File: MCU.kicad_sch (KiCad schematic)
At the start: 35 parts, among them J301 Conn_01x04_Pin, SW301 SW_Push, SW302 SW_Push, U301 STM32F405RGTx, Y301 24MHz

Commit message: refactor: change name from FeroFly405 to FeroFlyF405
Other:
- title: FeroFly405 -> FeroFlyF405
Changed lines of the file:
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@@
 	(paper "A4")
 	(title_block
-		(title "FeroFly405")
+		(title "FeroFlyF405")
 		(date "2026-07-22")
 		(rev "1")
-		(comment 3 "GitHub: https://github.com/Ozonised/FeroFly405")
+		(comment 3 "GitHub: https://github.com/Ozonised/FeroFlyF405")
 		(comment 4 "Designed by: Farhan Khan")
 	)
@@
 		)
 		(instances
-			(project "FeroFly"
+			(project "FeroFlyF405"
 				(path "/8fea5468-8d8d-4bdb-afc0-e65b62c92669/5f464b6b-c1a5-4802-8c09-16302411334a"
 					(reference "#PWR0314")
@@
 		)
 		(instances
-			(project "FeroFly"
+			(project "FeroFlyF405"
 				(path "/8fea5468-8d8d-4bdb-afc0-e65b62c92669/5f464b6b-c1a5-4802-8c09-16302411334a"
 					(reference "#PWR0307")
@@
 		)
 		(instances
-			(project "FeroFly"
+			(project "FeroFlyF405"
 				(path "/8fea5468-8d8d-4bdb-afc0-e65b62c92669/5f464b6b-c1a5-4802-8c09-16302411334a"
 					(reference "C307")
@@
 		)
 		(instances
-			(project "FeroFly"
+			(project "FeroFlyF405"
 				(path "/8fea5468-8d8d-4bdb-afc0-e65b62c92669/5f464b6b-c1a5-4802-8c09-16302411334a"
 					(reference "#PWR0305")
@@
 		)
 		(instances
-			(project "FeroFly"
+			(project "FeroFlyF405"
 				(path "/8fea5468-8d8d-4bdb-afc0-e65b62c92669/5f464b6b-c1a5-4802-8c09-16302411334a"
 					(reference "#PWR0303")
@@
 		)
 		(instances
-			(project "FeroFly"
+			(project "FeroFlyF405"
 				(path "/8fea5468-8d8d-4bdb-afc0-e65b62c92669/5f464b6b-c1a5-4802-8c09-16302411334a"
 					(reference "R303")
@@
 		)
 		(instances
-			(project "FeroFly"
+			(project "FeroFlyF405"
 				(path "/8fea5468-8d8d-4bdb-afc0-e65b62c92669/5f464b6b-c1a5-4802-8c09-16302411334a"
 					(reference "#PWR0304")
@@
 		)
 		(instances
-			(project "FeroFly"
+			(project "FeroFlyF405"
 				(path "/8fea5468-8d8d-4bdb-afc0-e65b62c92669/5f464b6b-c1a5-4802-8c09-16302411334a"
 					(reference "SW302")
@@
 		)
 		(instances
-			(project "FeroFly"
+			(project "FeroFlyF405"
 				(path "/8fea5468-8d8d-4bdb-afc0-e65b62c92669/5f464b6b-c1a5-4802-8c09-16302411334a"
 					(reference "R313")
@@
 		)
 		(instances
-			(project "FeroFly"
+			(project "FeroFlyF405"
 				(path "/8fea5468-8d8d-4bdb-afc0-e65b62c92669/5f464b6b-c1a5-4802-8c09-16302411334a"
 					(reference "R305")
@@
 		)
 		(instances
-			(project "FeroFly"
+			(project "FeroFlyF405"
 				(path "/8fea5468-8d8d-4bdb-afc0-e65b62c92669/5f464b6b-c1a5-4802-8c09-16302411334a"
 					(reference "R315")
@@
 		)
 		(instances
-			(project "FeroFly"
+			(project "FeroFlyF405"
 				(path "/8fea5468-8d8d-4bdb-afc0-e65b62c92669/5f464b6b-c1a5-4802-8c09-16302411334a"
 					(reference "#PWR0313")
@@
 		)
 		(instances
-			(project "FeroFly"
+			(project "FeroFlyF405"
 				(path "/8fea5468-8d8d-4bdb-afc0-e65b62c92669/5f464b6b-c1a5-4802-8c09-16302411334a"
 					(reference "C314")
@@
 		)
 		(instances
-			(project "FeroFly"
+			(project "FeroFlyF405"
 				(path "/8fea5468-8d8d-4bdb-afc0-e65b62c92669/5f464b6b-c1a5-4802-8c09-16302411334a"
 					(reference "C308")
@@
 		)
 		(instances
-			(project "FeroFly"
+			(project "FeroFlyF405"
 				(path "/8fea5468-8d8d-4bdb-afc0-e65b62c92669/5f464b6b-c1a5-4802-8c09-16302411334a"
 					(reference "R314")
@@
 		)
 		(instances
-			(project "FeroFly"
+			(project "FeroFlyF405"
 				(path "/8fea5468-8d8d-4bdb-afc0-e65b62c92669/5f464b6b-c1a5-4802-8c09-16302411334a"
 					(reference "R310")
@@
 		)
 		(instances
-			(project "FeroFly"
+			(project "FeroFlyF405"
 				(path "/8fea5468-8d8d-4bdb-afc0-e65b62c92669/5f464b6b-c1a5-4802-8c09-16302411334a"
 					(reference "#PWR0312")
@@
 		)
 		(instances
-			(project "FeroFly"
+			(project "FeroFlyF405"
 				(path "/8fea5468-8d8d-4bdb-afc0-e65b62c92669/5f464b6b-c1a5-4802-8c09-16302411334a"
 					(reference "C302")
@@
 		)
 		(instances
-			(project "FeroFly"
+			(project "FeroFlyF405"
 				(path "/8fea5468-8d8d-4bdb-afc0-e65b62c92669/5f464b6b-c1a5-4802-8c09-16302411334a"
 					(reference "R309")
@@
 		)
 		(instances
-			(project "FeroFly"
+			(project "FeroFlyF405"
 				(path "/8fea5468-8d8d-4bdb-afc0-e65b62c92669/5f464b6b-c1a5-4802-8c09-16302411334a"
 					(reference "#PWR0310")
@@
 		)
 		(instances
-			(project "FeroFly"
+			(project "FeroFlyF405"
 				(path "/8fea5468-8d8d-4bdb-afc0-e65b62c92669/5f464b6b-c1a5-4802-8c09-16302411334a"
 					(reference "C306")
@@
 		)
 		(instances
-			(project "FeroFly"
+			(project "FeroFlyF405"
 				(path "/8fea5468-8d8d-4bdb-afc0-e65b62c92669/5f464b6b-c1a5-4802-8c09-16302411334a"
 					(reference "J301")
@@
 		)
 		(instances
-			(project "FeroFly"
+			(project "FeroFlyF405"
 				(path "/8fea5468-8d8d-4bdb-afc0-e65b62c92669/5f464b6b-c1a5-4802-8c09-16302411334a"
 					(reference "#PWR0309")
@@
 		)
 		(instances
-			(project "FeroFly"
+			(project "FeroFlyF405"
 				(path "/8fea5468-8d8d-4bdb-afc0-e65b62c92669/5f464b6b-c1a5-4802-8c09-16302411334a"
 					(reference "R312")
@@
 		)
 		(instances
-			(project "FeroFly"
+			(project "FeroFlyF405"
 				(path "/8fea5468-8d8d-4bdb-afc0-e65b62c92669/5f464b6b-c1a5-4802-8c09-16302411334a"
 					(reference "R307")
@@
 		)
 		(instances
-			(project "FeroFly"
+			(project "FeroFlyF405"
 				(path "/8fea5468-8d8d-4bdb-afc0-e65b62c92669/5f464b6b-c1a5-4802-8c09-16302411334a"
 					(reference "C313")
@@
 		)
 		(instances
-			(project "FeroFly"
+			(project "FeroFlyF405"
 				(path "/8fea5468-8d8d-4bdb-afc0-e65b62c92669/5f464b6b-c1a5-4802-8c09-16302411334a"
 					(reference "#PWR0315")
@@
 		)
 		(instances
-			(project "FeroFly"
+			(project "FeroFlyF405"
 				(path "/8fea5468-8d8d-4bdb-afc0-e65b62c92669/5f464b6b-c1a5-4802-8c09-16302411334a"
 					(reference "C312")
@@
 		)
 		(instances
-			(project "FeroFly"
+			(project "FeroFlyF405"
 				(path "/8fea5468-8d8d-4bdb-afc0-e65b62c92669/5f464b6b-c1a5-4802-8c09-16302411334a"
 					(reference "C305")
@@
 		)
 		(instances
-			(project "FeroFly"
+			(project "FeroFlyF405"
 				(path "/8fea5468-8d8d-4bdb-afc0-e65b62c92669/5f464b6b-c1a5-4802-8c09-16302411334a"
 					(reference "U301")
@@
 		)
 		(instances
-			(project "FeroFly"
+			(project "FeroFlyF405"
 				(path "/8fea5468-8d8d-4bdb-afc0-e65b62c92669/5f464b6b-c1a5-4802-8c09-16302411334a"
 					(reference "R311")
@@
 		)
 		(instances
-			(project "FeroFly"
+			(project "FeroFlyF405"
 				(path "/8fea5468-8d8d-4bdb-afc0-e65b62c92669/5f464b6b-c1a5-4802-8c09-16302411334a"
 					(reference "#PWR0301")
@@
 		)
 		(instances
-			(project "FeroFly"
+			(project "FeroFlyF405"
 				(path "/8fea5468-8d8d-4bdb-afc0-e65b62c92669/5f464b6b-c1a5-4802-8c09-16302411334a"
 					(reference "#PWR0306")
@@
 		)
 		(instances
-			(project "FeroFly"
+			(project "FeroFlyF405"
 				(path "/8fea5468-8d8d-4bdb-afc0-e65b62c92669/5f464b6b-c1a5-4802-8c09-16302411334a"
 					(reference "C303")
@@
 		)
 		(instances
-			(project "FeroFly"
+			(project "FeroFlyF405"
 				(path "/8fea5468-8d8d-4bdb-afc0-e65b62c92669/5f464b6b-c1a5-4802-8c09-16302411334a"
 					(reference "#PWR0308")
@@
 		)
 		(instances
-			(project "FeroFly"
+			(project "FeroFlyF405"
 				(path "/8fea5468-8d8d-4bdb-afc0-e65b62c92669/5f464b6b-c1a5-4802-8c09-16302411334a"
 					(reference "R302")
@@
 		)
 		(instances
-			(project "FeroFly"
+			(project "FeroFlyF405"
 				(path "/8fea5468-8d8d-4bdb-afc0-e65b62c92669/5f464b6b-c1a5-4802-8c09-16302411334a"
 					(reference "C301")
@@
 		)
 		(instances
-			(project "FeroFly"
+			(project "FeroFlyF405"
 				(path "/8fea5468-8d8d-4bdb-afc0-e65b62c92669/5f464b6b-c1a5-4802-8c09-16302411334a"
 					(reference "SW301")
@@
 		)
 		(instances
-			(project "FeroFly"
+			(project "FeroFlyF405"
 				(path "/8fea5468-8d8d-4bdb-afc0-e65b62c92669/5f464b6b-c1a5-4802-8c09-16302411334a"
 					(reference "Y301")
@@
 		)
 		(instances
-			(project "FeroFly"
+			(project "FeroFlyF405"
 				(path "/8fea5468-8d8d-4bdb-afc0-e65b62c92669/5f464b6b-c1a5-4802-8c09-16302411334a"
 					(reference "#PWR0302")
@@
 		)
 		(instances
-			(project "FeroFly"
+			(project "FeroFlyF405"
 				(path "/8fea5468-8d8d-4bdb-afc0-e65b62c92669/5f464b6b-c1a5-4802-8c09-16302411334a"
 					(reference "C304")
@@
 		)
 		(instances
-			(project "FeroFly"
+			(project "FeroFlyF405"
 				(path "/8fea5468-8d8d-4bdb-afc0-e65b62c92669/5f464b6b-c1a5-4802-8c09-16302411334a"
 					(reference "R316")
@@
 		)
 		(instances
-			(project "FeroFly"
+			(project "FeroFlyF405"
 				(path "/8fea5468-8d8d-4bdb-afc0-e65b62c92669/5f464b6b-c1a5-4802-8c09-16302411334a"
 					(reference "C309")
@@
 		)
 		(instances
-			(project "FeroFly"
+			(project "FeroFlyF405"
 				(path "/8fea5468-8d8d-4bdb-afc0-e65b62c92669/5f464b6b-c1a5-4802-8c09-16302411334a"
 					(reference "R308")
@@
 		)
 		(instances
-			(project "FeroFly"
+			(project "FeroFlyF405"
 				(path "/8fea5468-8d8d-4bdb-afc0-e65b62c92669/5f464b6b-c1a5-4802-8c09-16302411334a"
 					(reference "#PWR0311")
@@
 		)
 		(instances
-			(project "FeroFly"
+			(project "FeroFlyF405"
 				(path "/8fea5468-8d8d-4bdb-afc0-e65b62c92669/5f464b6b-c1a5-4802-8c09-16302411334a"
 					(reference "C311")
@@
 		)
 		(instances
-			(project "FeroFly"
+			(project "FeroFlyF405"
 				(path "/8fea5468-8d8d-4bdb-afc0-e65b62c92669/5f464b6b-c1a5-4802-8c09-16302411334a"
 					(reference "R301")
@@
 		)
 		(instances
-			(project "FeroFly"
+			(project "FeroFlyF405"
 				(path "/8fea5468-8d8d-4bdb-afc0-e65b62c92669/5f464b6b-c1a5-4802-8c09-16302411334a"
 					(reference "R304")
@@
 		)
 		(instances
-			(project "FeroFly"
+			(project "FeroFlyF405"
 				(path "/8fea5468-8d8d-4bdb-afc0-e65b62c92669/5f464b6b-c1a5-4802-8c09-16302411334a"
 					(reference "R306")
@@
 		)
 		(instances
-			(project "FeroFly"
+			(project "FeroFlyF405"
 				(path "/8fea5468-8d8d-4bdb-afc0-e65b62c92669/5f464b6b-c1a5-4802-8c09-16302411334a"
 					(reference "C310")

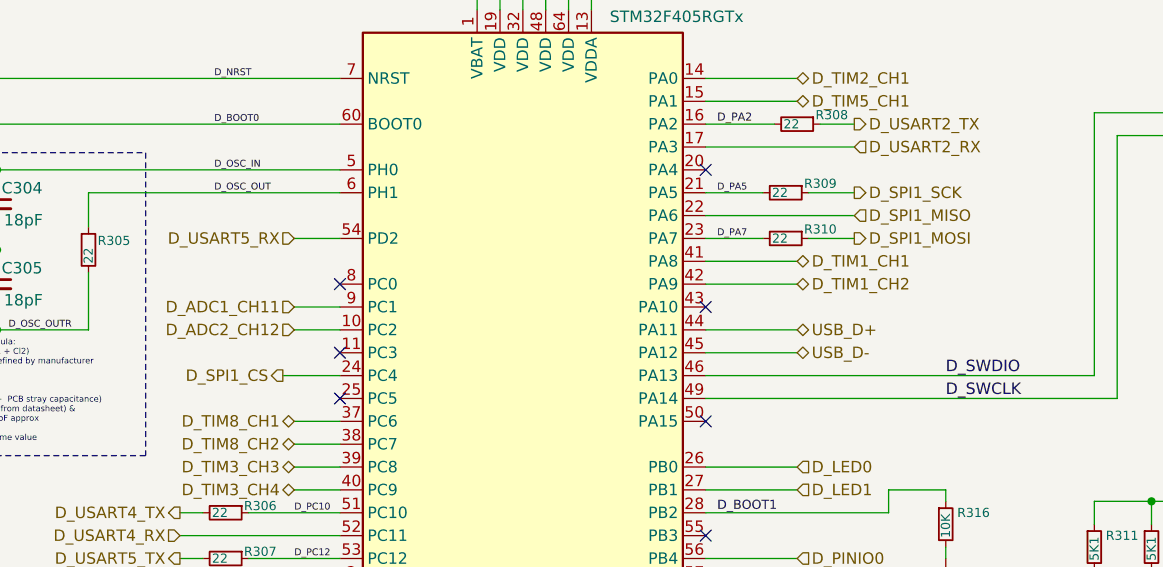
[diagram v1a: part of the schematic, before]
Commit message: refactor(schematic): assign net classes and fix USB net label assingment
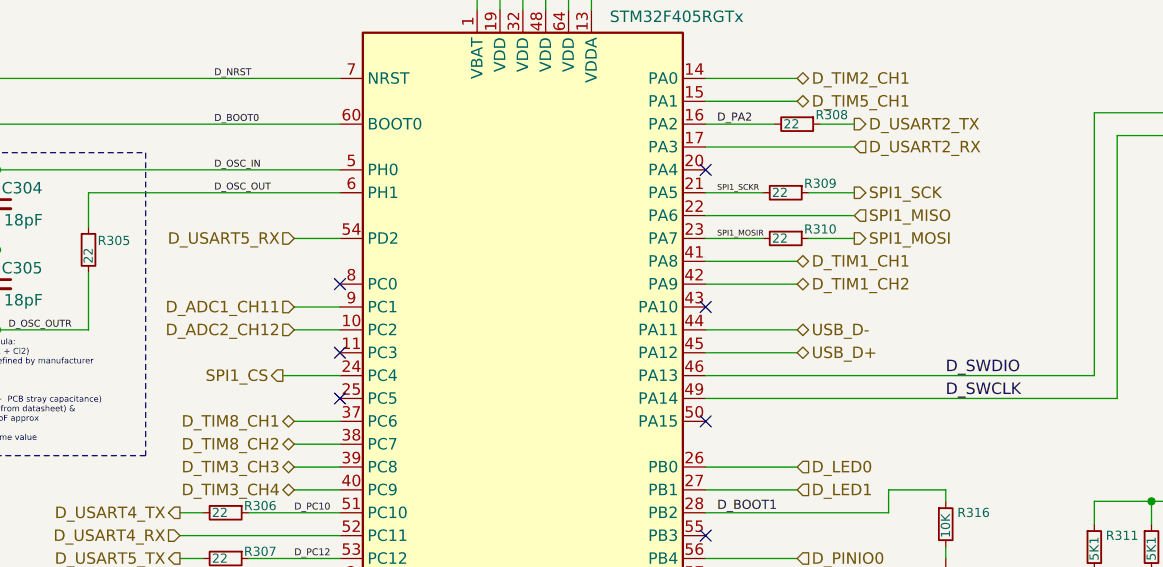
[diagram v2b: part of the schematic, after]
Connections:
- net USB_D+: now also U301.45 (PA12); no longer U301.44 (PA11)
- net USB_D-: now also U301.44 (PA11); no longer U301.45 (PA12)
- net D_PA5 renamed SPI1_SCKR
- net D_PA7 renamed SPI1_MOSIR
- net D_SPI1_CS renamed SPI1_CS
- net D_SPI1_MISO renamed SPI1_MISO
- net D_SPI1_MOSI renamed SPI1_MOSI
- net D_SPI1_SCK renamed SPI1_SCK

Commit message: refactor: change motor output, renamed power nets
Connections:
- net D_ADC1_CH11 is gone; now on net D_LED0: U301.9 (PC1)
- net D_ADC2_CH12 is gone; now on net D_LED1: U301.10 (PC2)
- net D_LED0: no longer U301.26 (PB0)
- net D_LED1: no longer U301.27 (PB1)
- net D_ADC2_CH13: now reaches U301.11 (PC3)
- net D_ADC1_CH10: now reaches U301.8 (PC0)
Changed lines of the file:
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@@
 	)
 	(no_connect
-		(at 134.62 104.14)
+		(at 175.26 119.38)
 	)
 	(no_connect
@@
 	)
 	(no_connect
-		(at 134.62 96.52)
+		(at 175.26 124.46)
 	)
 	(no_connect
-		(at 175.26 124.46)
+		(at 175.26 116.84)
 	)
 	(no_connect
@@
 	(wire
 		(pts
-			(xy 175.26 119.38) (xy 185.42 119.38)
-		)
-		(stroke
-			(width 0)
-			(type default)
-		)
-	)
-	(wire
-		(pts
 			(xy 218.44 123.19) (xy 218.44 120.65)
 		)
@@
 	(wire
 		(pts
+			(xy 129.54 104.14) (xy 134.62 104.14)
+		)
+		(stroke
+			(width 0)
+			(type default)
+		)
+	)
+	(wire
+		(pts
 			(xy 124.46 127) (xy 134.62 127)
 		)
@@
 	(wire
 		(pts
-			(xy 175.26 116.84) (xy 185.42 116.84)
-		)
-		(stroke
-			(width 0)
-			(type default)
-		)
-	)
-	(wire
-		(pts
 			(xy 74.93 78.74) (xy 74.93 97.79)
 		)
@@
 		(pts
 			(xy 60.96 97.79) (xy 63.5 97.79)
+		)
+		(stroke
+			(width 0)
+			(type default)
+		)
+	)
+	(wire
+		(pts
+			(xy 129.54 96.52) (xy 134.62 96.52)
 		)
 		(stroke
@@
 		)
 	)
+	(hierarchical_label "D_LED0"
+		(shape input)
+		(at 129.54 99.06 180)
+		(effects
+			(font
+				(size 1.27 1.27)
+			)
+			(justify right)
+		)
+	)
 	(hierarchical_label "D_CAN2TX"
 		(shape output)
@@
 		)
 	)
-	(hierarchical_label "D_LED0"
-		(shape input)
-		(at 185.42 116.84 0)
-		(effects
-			(font
-				(size 1.27 1.27)
-			)
-			(justify left)
-		)
-	)
 	(hierarchical_label "D_TIM4_CH3"
 		(shape bidirectional)
@@
 		)
 	)
+	(hierarchical_label "D_LED1"
+		(shape input)
+		(at 129.54 101.6 180)
+		(effects
+			(font
+				(size 1.27 1.27)
+			)
+			(justify right)
+		)
+	)
 	(hierarchical_label "D_TIM12_CH1"
 		(shape bidirectional)
@@
 		)
 	)
-	(hierarchical_label "D_LED1"
-		(shape input)
-		(at 185.42 119.38 0)
-		(effects
-			(font
-				(size 1.27 1.27)
-			)
-			(justify left)
-		)
-	)
 	(hierarchical_label "D_PINIO1"
 		(shape input)
@@
 		)
 	)
-	(hierarchical_label "D_ADC2_CH12"
+	(hierarchical_label "D_ADC2_CH13"
 		(shape input)
-		(at 129.54 101.6 180)
+		(at 129.54 104.14 180)
 		(effects
 			(font
@@
 		)
 	)
-	(hierarchical_label "D_ADC1_CH11"
+	(hierarchical_label "D_ADC1_CH10"
 		(shape input)
-		(at 129.54 99.06 180)
-		(effects
-			(font
+		(at 129.54 96.52 180)
+		(effects
+			(font

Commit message: feat:  change SWD connector, route SWD signal & LEDs
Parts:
- removed J301: Conn_01x04_Pin, Connector_PinHeader_2.54mm:PinHeader_1x04_P2.54mm_Vertical, symbol Connector:Conn_01x04_Pin
- added J302: SM04B-GHS-TB(LF)(SN), Connector_JST:JST_GH_SM04B-GHS-TB_1x04-1MP_P1.25mm_Horizontal, symbol Connector_Generic_MountingPin:Conn_01x04_MountingPin
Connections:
- net +3V3: now also J302.1 (Pin_1)
- net D_LED1: now also U301.50 (PA15); no longer U301.10 (PC2)
- net D_SWCLK: now also J302.3 (Pin_3)
- net D_SWDIO: now also J302.2 (Pin_2)
- net GND: now also J302.4 (Pin_4), J302.MP (MountPin)
